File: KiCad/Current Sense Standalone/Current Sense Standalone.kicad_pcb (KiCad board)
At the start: 2 copper layers, 62.3 x 24.3 mm, 10 parts, among them J1 PLUG INPUT BATTERY IN HERE (X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, J3 V+/- TEST Header PIN, J4 BAT +TERMINAL TEST HEADER PIN, J6 to MCU GPIO PIN, J7 PLUG BATTERY OUTPUT HERE (XT6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, U1 INA139QPWRQ1

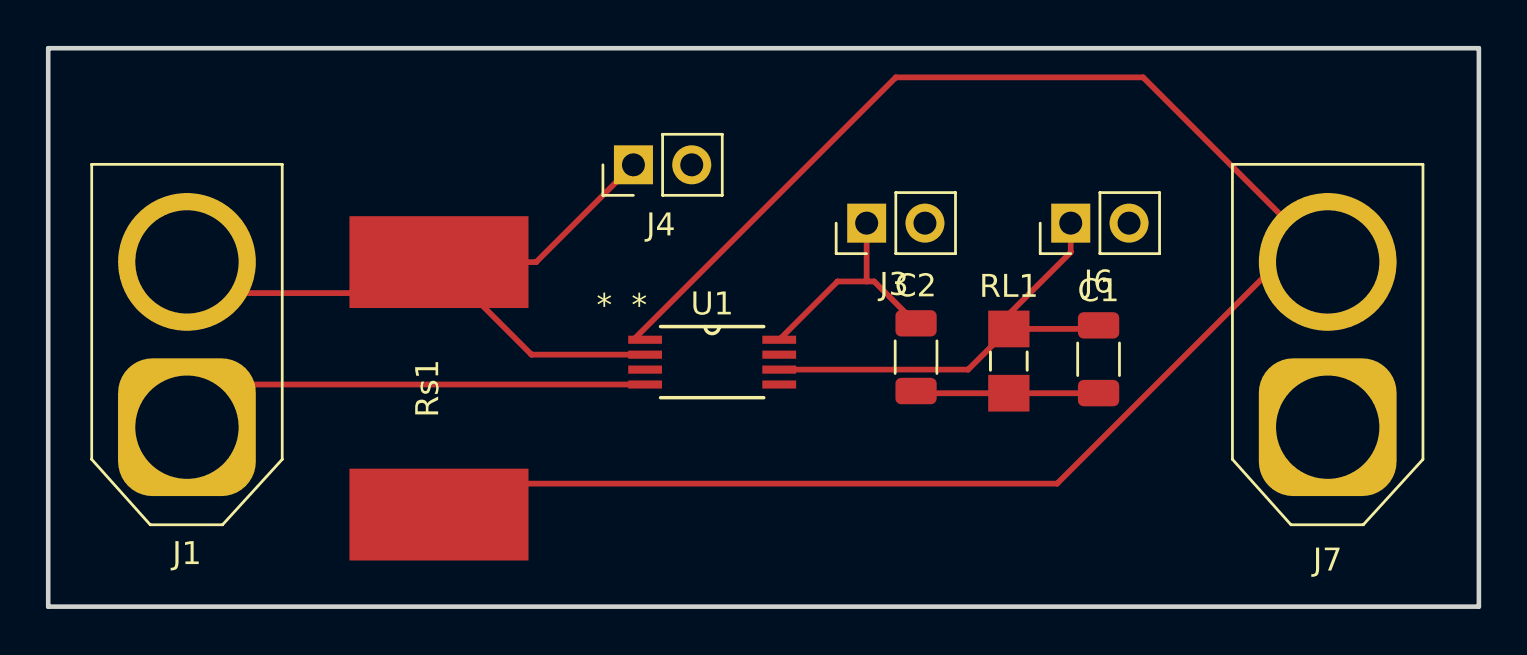
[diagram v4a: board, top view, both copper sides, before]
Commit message: Made traces a bit thicker for current sense
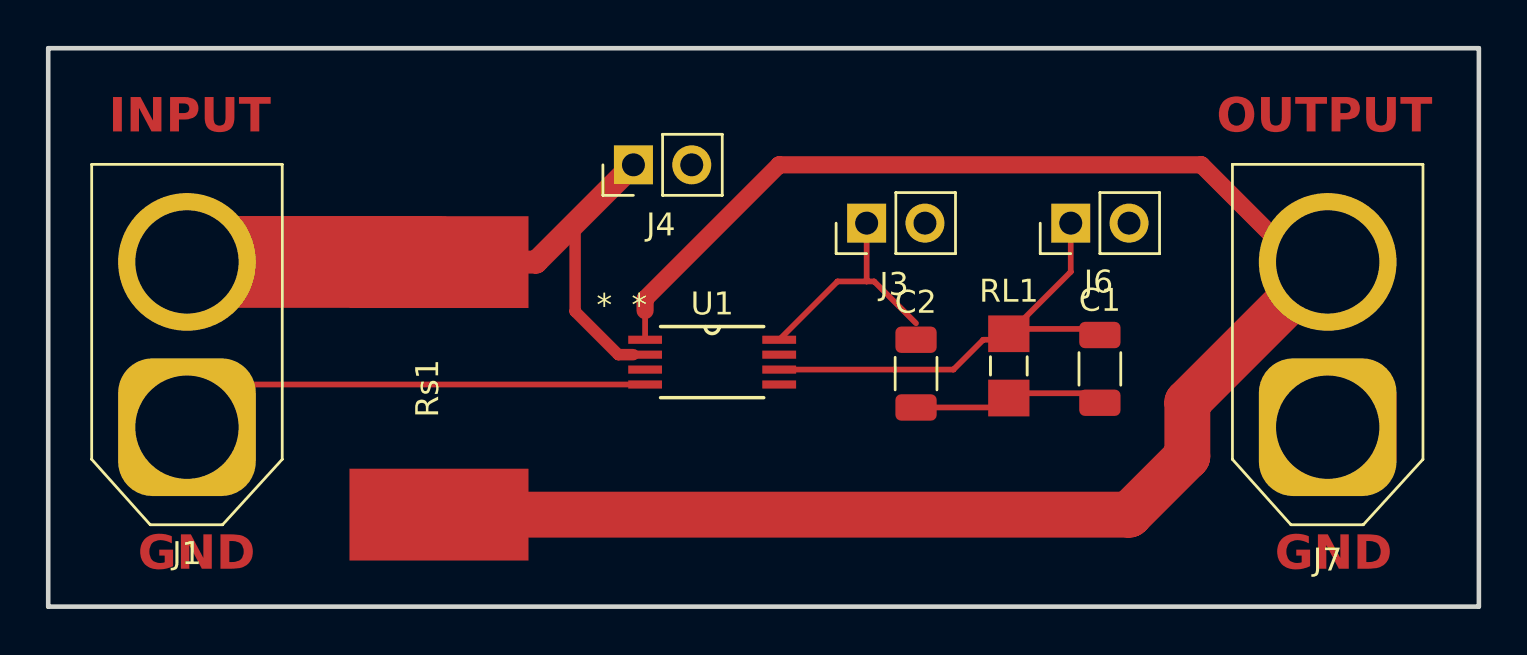
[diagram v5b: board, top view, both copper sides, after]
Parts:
- moved C2 0.72 mm to (50.4, 26.9)
- moved C1 0.42 mm to (58.4, 26.7)
- moved RL1 0.21 mm to (54.5, 26.5)
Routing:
- net /Batt-: track 81.0 -> 82.5 mm
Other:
- board text added: "GND"
- board text added: "INPUT"
- board text added: "OUTPUT"
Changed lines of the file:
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@@
       (drillshape 0)
       (scaleselection 1)
-      (outputdirectory "Gerbers/8-24-23/")
+      (outputdirectory "Gerbers/8-26-23/")
     )
   )
@@
   )
   (footprint "Capacitor_SMD:C_1206_3216Metric" (layer "F.Cu")
-    (at 50.411329 26.158866 -90)
+    (at 50.411329 26.875 -90)
     (descr "Capacitor SMD 1206 (3216 Metric), square (rectangular) end terminal, IPC_7351 nominal, (Body size source: IPC-SM-782 page 76, https://www.pcb-3d.com/wordpress/wp-content/uploads/ipc-sm-782a_amendment_1_and_2.pdf), generated with kicad-footprint-generator")
     (tags "capacitor")
@@
   )
   (footprint "RC1206FR-13100KL:RESC3216X65" (layer "F.Cu")
-    (at 54.453375 26.329624 -90)
+    (at 54.453375 26.54 -90)
     (descr "<b>RESISTOR</b>")
     (property "Sheetfile" "Current Sense Standalone.kicad_sch")
@@
   )
   (footprint "Capacitor_SMD:C_1206_3216Metric" (layer "F.Cu")
-    (at 58.363078 26.249784 -90)
+    (at 58.42 26.67 -90)
     (descr "Capacitor SMD 1206 (3216 Metric), square (rectangular) end terminal, IPC_7351 nominal, (Body size source: IPC-SM-782 page 76, https://www.pcb-3d.com/wordpress/wp-content/uploads/ipc-sm-782a_amendment_1_and_2.pdf), generated with kicad-footprint-generator")
     (tags "capacitor")
@@
   (gr_rect (start 12.606153 12.7) (end 74.93 37.026478)
     (stroke (width 0.2) (type default)) (fill none) (layer "Edge.Cuts"))
-  (segment (start 54.453375 24.286625) (end 54.453375 24.929624) (width 0.25) (layer "F.Cu") (net 1))
-  (segment (start 52.682999 26.7) (end 54.453375 24.929624) (width 0.25) (layer "F.Cu") (net 1))
-  (segment (start 44.45 26.7) (end 52.682999 26.7) (width 0.25) (layer "F.Cu") (net 1))
-  (segment (start 57.15 20.32) (end 57.15 21.59) (width 0.25) (layer "F.Cu") (net 1))
-  (segment (start 57.15 21.59) (end 54.453375 24.286625) (width 0.25) (layer "F.Cu") (net 1))
+  (gr_text "GND" (at 16.51 35.56) (layer "F.Cu")
+    (effects (font (size 1.5 1.5) (thickness 0.3) bold) (justify left bottom))
+  )
+  (gr_text "GND\n" (at 66.04 35.56) (layer "F.Cu")
+    (effects (font (size 1.5 1.5) (thickness 0.3) bold) (justify left bottom))
+  )
+  (gr_text "OUTPUT" (at 63.5 16.51) (layer "F.Cu")
+    (effects (font (size 1.5 1.5) (thickness 0.3) bold) (justify left bottom))
+  )
+  (gr_text "INPUT" (at 15.24 16.51) (layer "F.Cu")
+    (effects (font (size 1.5 1.5) (thickness 0.3) bold) (justify left bottom))
+  )
+  (segment (start 57.15 20.32) (end 57.15 22.443375) (width 0.25) (layer "F.Cu") (net 1))
+  (segment (start 57.15 22.443375) (end 54.663751 24.929624) (width 0.25) (layer "F.Cu") (net 1))
+  (segment (start 54.663751 24.929624) (end 54.453375 24.929624) (width 0.25) (layer "F.Cu") (net 1))
+  (segment (start 53.34 25.4) (end 53.982999 25.4) (width 0.25) (layer "F.Cu") (net 1))
+  (segment (start 44.45 26.7) (end 52.04 26.7) (width 0.25) (layer "F.Cu") (net 1))
+  (segment (start 53.982999 25.4) (end 54.453375 24.929624) (width 0.25) (layer "F.Cu") (net 1))
   (segment (start 58.208238 24.929624) (end 58.363078 24.774784) (width 0.25) (layer "F.Cu") (net 1))
   (segment (start 54.453375 24.929624) (end 58.208238 24.929624) (width 0.25) (layer "F.Cu") (net 1))
-  (segment (start 50.507087 27.729624) (end 50.411329 27.633866) (width 0.25) (layer "F.Cu") (net 2))
+  (segment (start 52.04 26.7) (end 53.34 25.4) (width 0.25) (layer "F.Cu") (net 1))
+  (segment (start 58.363078 27.724784) (end 58.358238 27.729624) (width 0.25) (layer "F.Cu") (net 2))
+  (segment (start 58.358238 27.729624) (end 54.663751 27.729624) (width 0.25) (layer "F.Cu") (net 2))
   (segment (start 18.650936 29.21) (end 20.510938 27.349998) (width 0.25) (layer "F.Cu") (net 2))
-  (segment (start 58.358238 27.729624) (end 54.453375 27.729624) (width 0.25) (layer "F.Cu") (net 2))
-  (segment (start 58.363078 27.724784) (end 58.358238 27.729624) (width 0.25) (layer "F.Cu") (net 2))
   (segment (start 20.510938 27.349998) (end 38.608 27.349998) (width 0.25) (layer "F.Cu") (net 2))
-  (segment (start 54.453375 27.729624) (end 50.507087 27.729624) (width 0.25) (layer "F.Cu") (net 2))
+  (segment (start 54.663751 27.729624) (end 54.043375 28.35) (width 0.25) (layer "F.Cu") (net 2))
+  (segment (start 54.043375 28.35) (end 50.411329 28.35) (width 0.25) (layer "F.Cu") (net 2))
   (segment (start 44.45 25.4) (end 46.99 22.86) (width 0.25) (layer "F.Cu") (net 3))
   (segment (start 48.26 22.86) (end 48.26 20.32) (width 0.25) (layer "F.Cu") (net 3))
@@
   (segment (start 48.587463 22.86) (end 50.411329 24.683866) (width 0.25) (layer "F.Cu") (net 3))
   (segment (start 48.26 22.86) (end 48.587463 22.86) (width 0.25) (layer "F.Cu") (net 3))
-  (segment (start 29.629273 22.018011) (end 33.66126 26.049998) (width 0.25) (layer "F.Cu") (net 7))
-  (segment (start 33.66126 26.049998) (end 38.608 26.049998) (width 0.25) (layer "F.Cu") (net 7))
-  (segment (start 38.1 17.78) (end 33.861989 22.018011) (width 0.25) (layer "F.Cu") (net 7))
+  (segment (start 38.1 26.049998) (end 37.443598 26.049998) (width 0.5) (layer "F.Cu") (net 7))
+  (segment (start 38.1 17.78) (end 33.861989 22.018011) (width 1) (layer "F.Cu") (net 7))
   (segment (start 28.279273 23.368011) (end 29.629273 22.018011) (width 0.25) (layer "F.Cu") (net 7))
+  (segment (start 38.1 26.049998) (end 38.608 26.049998) (width 0.25) (layer "F.Cu") (net 7))
+  (segment (start 29.621262 22.01) (end 29.629273 22.018011) (width 0.25) (layer "F.Cu") (net 7))
   (segment (start 18.650936 22.01) (end 20.008947 23.368011) (width 0.25) (layer "F.Cu") (net 7))
-  (segment (start 20.008947 23.368011) (end 28.279273 23.368011) (width 0.25) (layer "F.Cu") (net 7))
-  (segment (start 33.861989 22.018011) (end 29.629273 22.018011) (width 0.25) (layer "F.Cu") (net 7))
+  (segment (start 33.861989 22.018011) (end 29.629273 22.018011) (width 1) (layer "F.Cu") (net 7))
+  (segment (start 37.443598 26.049998) (end 35.56 24.1664) (width 0.5) (layer "F.Cu") (net 7))
+  (segment (start 35.56 24.1664) (end 35.56 20.32) (width 0.5) (layer "F.Cu") (net 7))
   (segment (start 18.650936 20.130973) (end 18.650936 22.01) (width 0.25) (layer "F.Cu") (net 7))
-  (segment (start 49.53 13.97) (end 38.1 25.4) (width 0.25) (layer "F.Cu") (net 8))
-  (segment (start 56.557856 31.668011) (end 66.215867 22.01) (width 0.25) (layer "F.Cu") (net 8))
-  (segment (start 60.304045 13.97) (end 49.53 13.97) (width 0.25) (layer "F.Cu") (net 8))
+  (segment (start 18.650936 22.01) (end 29.621262 22.01) (width 4) (layer "F.Cu") (net 7))
+  (segment (start 59.69 33.02) (end 62.23 30.48) (width 2) (layer "F.Cu") (net 8))
+  (segment (start 38.608 23.622) (end 44.45 17.78) (width 0.75) (layer "F.Cu") (net 8))
+  (segment (start 38.608 24.13) (end 38.608 25.4) (width 0.25) (layer "F.Cu") (net 8))
   (segment (start 66.215867 22.01) (end 68.344045 22.01) (width 0.25) (layer "F.Cu") (net 8))
-  (segment (start 29.629273 31.668011) (end 56.557856 31.668011) (width 0.25) (layer "F.Cu") (net 8))
-  (segment (start 68.344045 22.01) (end 60.304045 13.97) (width 0.25) (layer "F.Cu") (net 8))
+  (segment (start 62.23 30.48) (end 62.23 28.124045) (width 2) (layer "F.Cu") (net 8))
+  (segment (start 38.608 24.13) (end 38.608 23.622) (width 0.75) (layer "F.Cu") (net 8))
+  (segment (start 29.631262 33.02) (end 59.69 33.02) (width 2) (layer "F.Cu") (net 8))
+  (segment (start 29.629273 33.018011) (end 29.631262 33.02) (width 2) (layer "F.Cu") (net 8))
+  (segment (start 68.344045 22.01) (end 67.074045 22.01) (width 0.25) (layer "F.Cu") (net 8))
+  (segment (start 44.45 17.78) (end 62.844045 17.78) (width 0.75) (layer "F.Cu") (net 8))
+  (segment (start 62.844045 17.78) (end 67.074045 22.01) (width 0.75) (layer "F.Cu") (net 8))
+  (segment (start 62.23 28.124045) (end 68.344045 22.01) (width 2) (layer "F.Cu") (net 8))
   (zone (net 2) (net_name "GND") (layers "F&B.Cu") (hatch edge 0.5)
     (connect_pads yes (clearance 0.5))

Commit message: tweaked traces
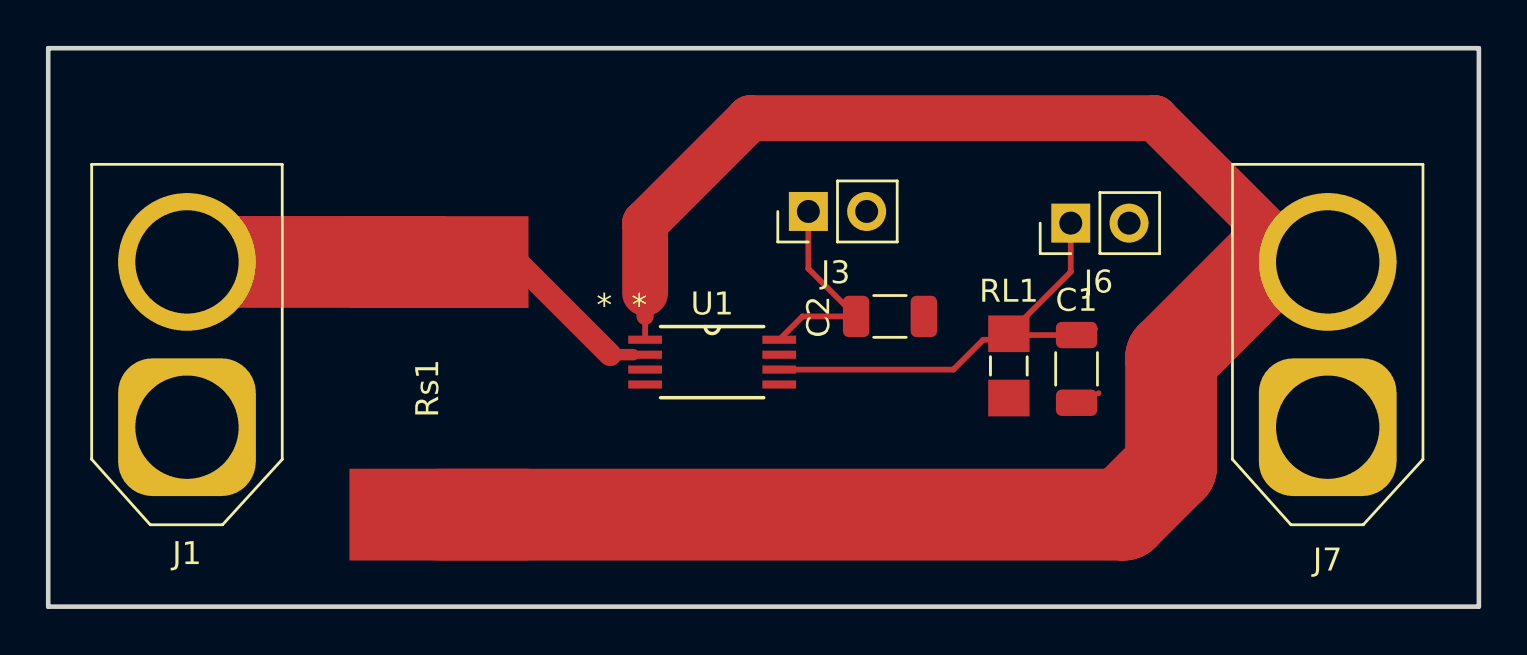
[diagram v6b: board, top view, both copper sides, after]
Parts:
- removed J4: BAT +TERMINAL TEST HEADER PIN, Connector_PinHeader_2.54mm:PinHeader_1x02_P2.54mm_Vertical
- moved C2 2.74 mm to (49.3, 24.4), turned to 0 degrees
- moved J3 2.59 mm to (45.7, 19.8)
- moved C1 1.02 mm to (57.4, 26.7)
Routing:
- net GND: track 28.9 -> 3.51 mm
- net /Batt+: track 34.6 -> 27.3 mm
- net /Batt-: track 82.5 -> 84.1 mm
- net /V-: track 10.3 -> 9.21 mm
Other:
- board text removed: "GND"
- board text removed: "INPUT"
- board text removed: "OUTPUT"
